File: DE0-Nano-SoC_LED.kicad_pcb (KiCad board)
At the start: 2 copper layers, 10 parts, among them J1 Conn_02x08_Odd_Even, J2 Conn_02x08_Odd_Even, J3 Conn_02x20_Odd_Even, J4 Conn_02x20_Odd_Even, U1 74HC245, U2 74HC245

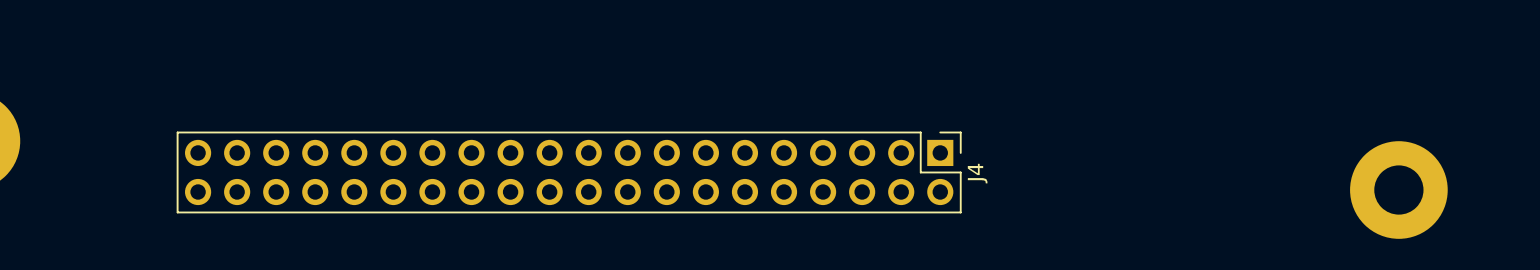
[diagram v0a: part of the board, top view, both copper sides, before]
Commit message: main DE0-Nano-SoC connectors are finally locked in their places
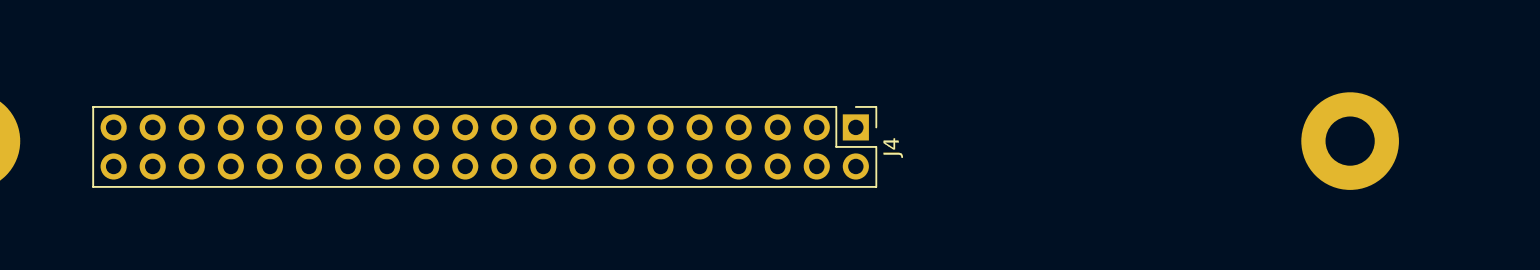
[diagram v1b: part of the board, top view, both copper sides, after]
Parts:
- moved J4 5.74 mm to (127.5, 131.3)
- moved REF** 4.61 mm to (159.7, 132.2)
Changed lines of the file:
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@@
     (links 10)
     (no_connects 10)
-    (area 69.899999 19.498 252.575001 143.322382)
+    (area 50.880001 18.804999 252.575001 142.922382)
     (thickness 1.6)
-    (drawings 3)
+    (drawings 9)
     (tracks 0)
     (zones 0)
@@
     )
   )
-  (module Pin_Headers:Pin_Header_Straight_2x20_Pitch2.54mm (layer F.Cu)
+  (module Pin_Headers:Pin_Header_Straight_2x20_Pitch2.54mm locked (layer F.Cu)
     (at 79.25 70.89 90)
     (descr "Through hole straight pin header, 2x20, 2.54mm pitch, double rows")
@@
     )
   )
-  (module Pin_Headers:Pin_Header_Straight_2x20_Pitch2.54mm (layer F.Cu)
-    (at 133 133 270)
+  (module Pin_Headers:Pin_Header_Straight_2x20_Pitch2.54mm locked (layer F.Cu)
+    (at 127.51 131.34 270)
     (descr "Through hole straight pin header, 2x20, 2.54mm pitch, double rows")
     (tags "Through hole pin header THT 2x20 2.54mm double row")
@@
   )
   (module wire_pad_custom:VIA-3.2x6.35mm (layer F.Cu)
-    (at 162.9 135.5)
+    (at 159.65 132.23)
     (fp_text reference REF** (at 0 4) (layer F.SilkS) hide
       (effects (font (size 1 1) (thickness 0.15)))
@@
       (effects (font (size 1 1) (thickness 0.15)))
     )
-    (pad 1 thru_hole circle (at -0.08 -0.09) (size 6.35 6.35) (drill 3.2) (layers *.Cu *.Mask)
+    (pad 1 thru_hole circle (at 0 0) (size 6.35 6.35) (drill 3.2) (layers *.Cu *.Mask)
       (net 42 GND))
   )
+  (gr_line (start 162.83 66.82) (end 162.83 135.41) (angle 90) (layer Eco1.User) (width 0.05))
+  (gr_line (start 66.82 66.82) (end 162.83 66.82) (angle 90) (layer Eco1.User) (width 0.05))
+  (gr_line (start 66.82 135.41) (end 162.83 135.41) (angle 90) (layer Eco1.User) (width 0.05))
+  (gr_line (start 66.82 66.82) (end 66.82 135.41) (angle 90) (layer Eco1.User) (width 0.05))
+  (dimension 57.51 (width 0.3) (layer Eco1.User)
+    (gr_text "57,510 mm" (at 98.755 123.82) (layer Eco1.User)
+      (effects (font (size 1.5 1.5) (thickness 0.3)))
+    )
+    (feature1 (pts (xy 127.51 132.23) (xy 127.51 122.47)))
+    (feature2 (pts (xy 70 132.23) (xy 70 122.47)))
+    (crossbar (pts (xy 70 125.17) (xy 127.51 125.17)))
+    (arrow1a (pts (xy 127.51 125.17) (xy 126.383496 125.756421)))
+    (arrow1b (pts (xy 127.51 125.17) (xy 126.383496 124.583579)))
+    (arrow2a (pts (xy 70 125.17) (xy 71.126504 125.756421)))
+    (arrow2b (pts (xy 70 125.17) (xy 71.126504 124.583579)))
+  )
+  (dimension 89.65 (width 0.3) (layer Eco1.User)
+    (gr_text "89,650 mm" (at 114.825 144.23) (layer Eco1.User)
+      (effects (font (size 1.5 1.5) (thickness 0.3)))
+    )
+    (feature1 (pts (xy 159.65 132.23) (xy 159.65 145.58)))
+    (feature2 (pts (xy 70 132.23) (xy 70 145.58)))
+    (crossbar (pts (xy 70 142.88) (xy 159.65 142.88)))
+    (arrow1a (pts (xy 159.65 142.88) (xy 158.523496 143.466421)))
+    (arrow1b (pts (xy 159.65 142.88) (xy 158.523496 142.293579)))
+    (arrow2a (pts (xy 70 142.88) (xy 71.126504 143.466421)))
+    (arrow2b (pts (xy 70 142.88) (xy 71.126504 142.293579)))
+  )
   (dimension 62.23 (width 0.3) (layer Eco1.User)

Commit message: still in connectors placement phase
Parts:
- removed REF** (x4): VIA-3.2x6.35mm, wire_pad_custom:VIA-3.2x6.35mm
- added J10: Conn_01x01, Mounting_Holes:MountingHole_3.2mm_M3_ISO7380_Pad, F.Cu at (70.0, 132.2)
- added J11: Conn_01x01, Mounting_Holes:MountingHole_3.2mm_M3_ISO7380_Pad, F.Cu at (159.7, 70.0)
- added J12: Conn_01x01, Mounting_Holes:MountingHole_3.2mm_M3_ISO7380_Pad, F.Cu at (69.5, 189.8)
- added J13: Conn_01x01, Mounting_Holes:MountingHole_3.2mm_M3_ISO7380_Pad, F.Cu at (158.3, 190.8)
- added J14: Conn_01x01, Mounting_Holes:MountingHole_3.2mm_M3_ISO7380_Pad, F.Cu at (70.0, 20.0)
- added J15: Conn_01x01, Mounting_Holes:MountingHole_3.2mm_M3_ISO7380_Pad, F.Cu at (159.7, 20.0)
- added J16: Conn_01x10, Pin_Headers:Pin_Header_Straight_1x10_Pitch2.54mm, F.Cu at (80.5, 79.0)
- added J17: Conn_01x08, Pin_Headers:Pin_Header_Straight_1x08_Pitch2.54mm, F.Cu at (108.9, 78.9)
- added J18: Conn_01x06, Pin_Headers:Pin_Header_Straight_1x06_Pitch2.54mm, F.Cu at (110.9, 120.3)
- added J19: Conn_01x08, Pin_Headers:Pin_Header_Straight_1x08_Pitch2.54mm, F.Cu at (88.0, 120.2)
- added J5: Conn_02x08_Odd_Even, Connectors_Multicomp:Multicomp_MC9A12-1634_2x08x2.54mm_Straight, F.Cu at (98.0, 45.0)
- added J6: Conn_02x08_Odd_Even, Connectors_Multicomp:Multicomp_MC9A12-1634_2x08x2.54mm_Straight, F.Cu at (134.0, 45.0)
- added J7: Conn_02x08_Odd_Even, Connectors_Multicomp:Multicomp_MC9A12-1634_2x08x2.54mm_Straight, F.Cu at (152.0, 45.0)
- added J8: Conn_01x01, Mounting_Holes:MountingHole_3.2mm_M3_ISO7380_Pad, F.Cu at (70.0, 70.0)
- added J9: Conn_01x01, Mounting_Holes:MountingHole_3.2mm_M3_ISO7380_Pad, F.Cu at (159.7, 132.2)
- added RN1: R_Pack04, Resistors_SMD:R_Array_Concave_4x0402, F.Cu at (105.1, 60.1)
- added RN2: R_Pack04, Resistors_SMD:R_Array_Concave_4x0402, F.Cu at (107.8, 60.1)
- moved J2 126.1 mm to (116.0, 45.0), turned to 90 degrees
- moved U1 41.4 mm to (106.5, 54.6)
- moved U2 38.5 mm to (80.2, 55.2)
- moved J1 2.68 mm to (79.0, 45.0)
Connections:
- J1 pad 16: Net-(J1-Pad16) -> GND
- J1 pad 4: Net-(J1-Pad4) -> GND
- J1 pad 8: Net-(J1-Pad8) -> GND
- J2 pad 16: Net-(J2-Pad16) -> GND
- J2 pad 4: Net-(J2-Pad4) -> GND
- J2 pad 8: Net-(J2-Pad8) -> GND
- J3 pad 11: Net-(J3-Pad11) -> VCC
- J3 pad 29: Net-(J3-Pad29) -> /3V3
- J4 pad 11: Net-(J4-Pad11) -> VCC
- J4 pad 29: Net-(J4-Pad29) -> /3V3
- U1 pad 1: Net-(U1-Pad1) -> VCC
- U1 pad 19: Net-(U1-Pad19) -> GND
- U2 pad 1: Net-(U2-Pad1) -> VCC
- U2 pad 19: Net-(U2-Pad19) -> GND
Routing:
- added copper zone on F.Cu, net GND
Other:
- board outline added: 98.1 x 178.3 mm
- net class Default: clearance 0.2 -> 0.18; trace_width 0.25 -> 0.18; via_dia 0.6 -> 0.7; via_drill 0.4 -> 0.3
- rule trace_clearance: 0.2 -> 0.18
- rule trace_min: 0.2 -> 0.18
- rule via_min_size: 0.4 -> 0.7

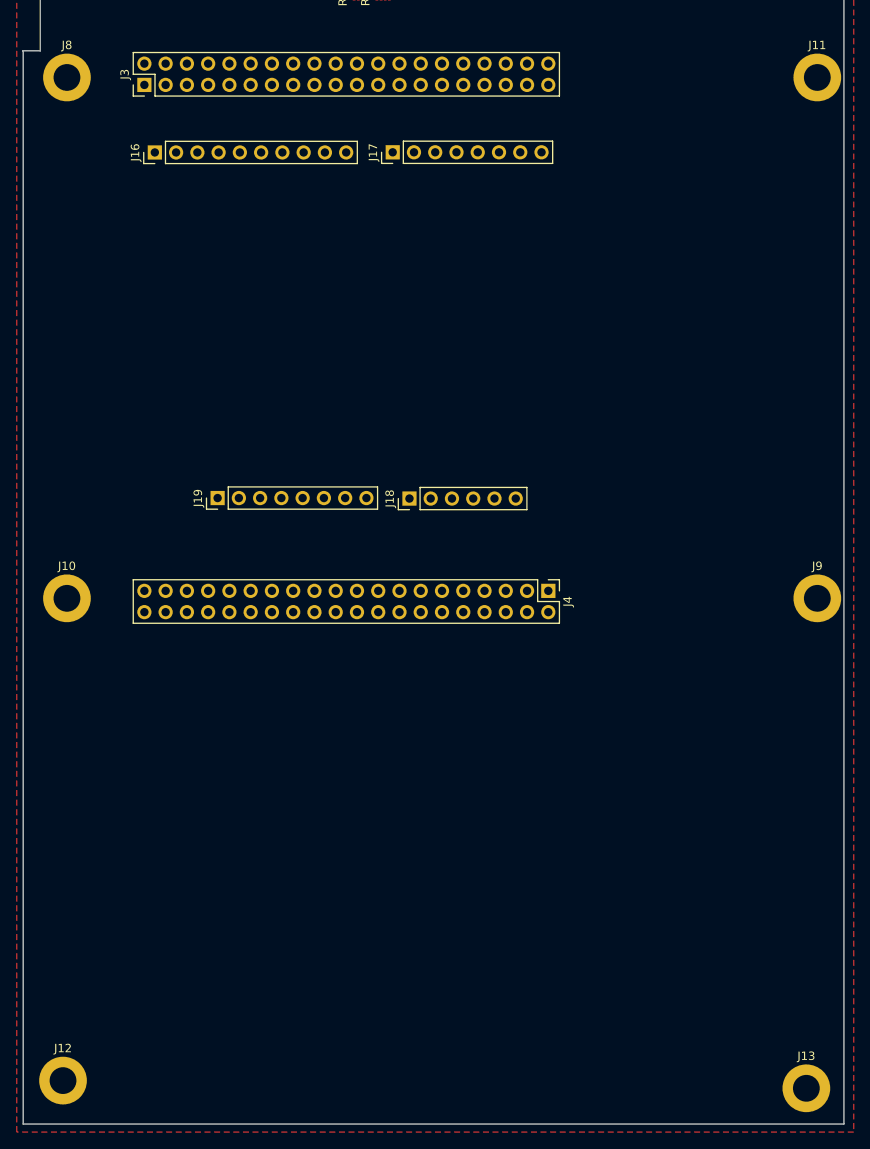
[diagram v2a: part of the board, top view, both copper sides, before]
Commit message: add more connectors
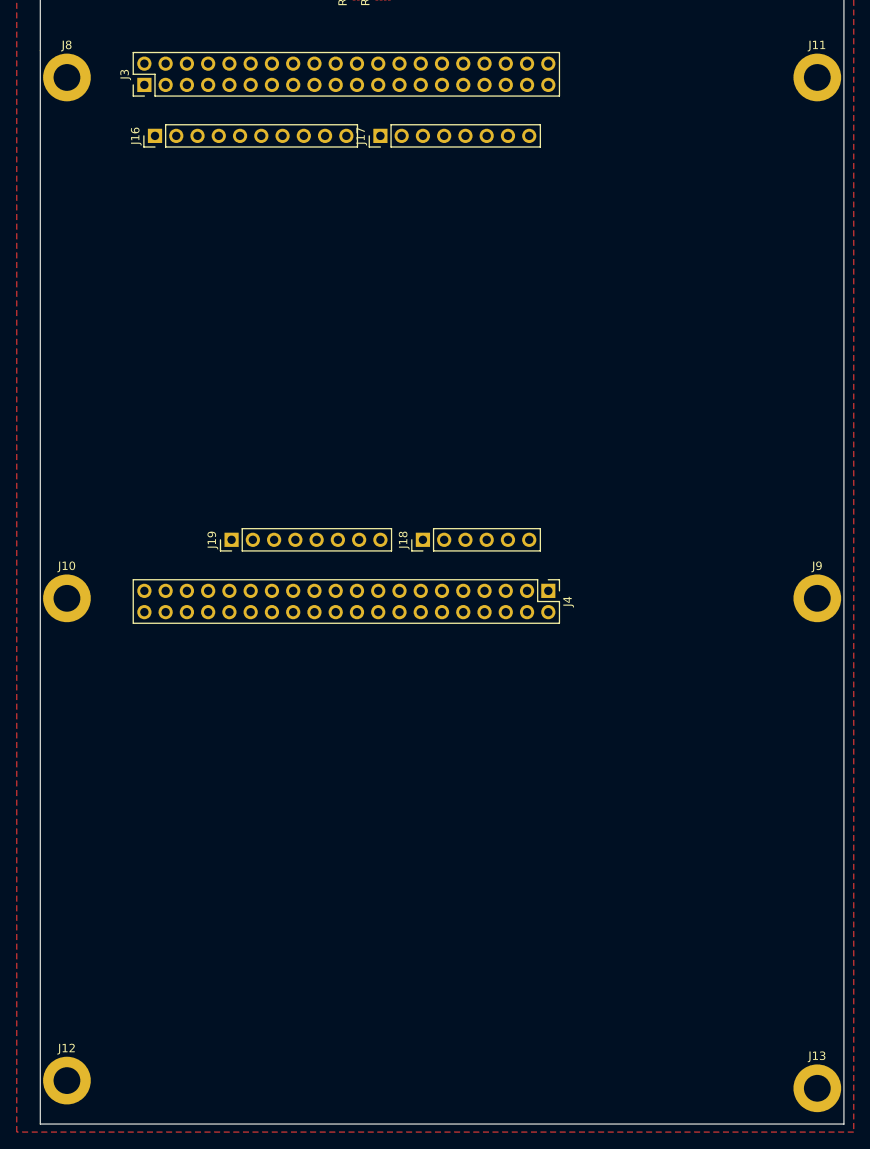
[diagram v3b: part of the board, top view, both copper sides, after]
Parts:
- moved J19 5.26 mm to (89.7, 125.2)
- moved J18 5.19 mm to (112.5, 125.2)
- moved J17 2.45 mm to (107.5, 77.0)
- moved J16 1.98 mm to (80.5, 77.0)
- moved J13 1.31 mm to (159.7, 190.8)
- moved J12 0.47 mm to (70.0, 189.8)
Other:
- board size 98.1 x 178.3 mm -> 96 x 178.3 mm
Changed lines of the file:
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@@
     (links 50)
     (no_connects 50)
-    (area 64.694999 16.754999 162.905001 195.115001)
+    (area 50.880001 15.195 164.37762 196.000001)
     (thickness 1.6)
-    (drawings 19)
+    (drawings 23)
     (tracks 0)
     (zones 0)
@@
     (37 F.SilkS user)
     (38 B.Mask user)
-    (39 F.Mask user)
+    (39 F.Mask user hide)
     (40 Dwgs.User user)
     (41 Cmts.User user)
@@
     (pad_to_mask_clearance 0.2)
     (aux_axis_origin 0 0)
+    (grid_origin 10.05 199.94)
     (visible_elements FFFFF75F)
     (pcbplotparams
@@
   )
   (module Mounting_Holes:MountingHole_3.2mm_M3_ISO7380_Pad (layer F.Cu)
-    (at 69.53 189.85)
+    (at 70 189.85)
     (descr "Mounting Hole 3.2mm, M3, ISO7380")
     (tags "mounting hole 3.2mm m3 iso7380")
@@
   )
   (module Mounting_Holes:MountingHole_3.2mm_M3_ISO7380_Pad (layer F.Cu)
-    (at 158.34 190.77)
+    (at 159.65 190.77)
     (descr "Mounting Hole 3.2mm, M3, ISO7380")
     (tags "mounting hole 3.2mm m3 iso7380")
@@
       (net 27 GND))
   )
-  (module Pin_Headers:Pin_Header_Straight_1x10_Pitch2.54mm (layer F.Cu)
-    (at 80.5 78.96 90)
+  (module Pin_Headers:Pin_Header_Straight_1x10_Pitch2.54mm locked (layer F.Cu)
+    (at 80.52 76.98 90)
     (descr "Through hole straight pin header, 1x10, 2.54mm pitch, single row")
     (tags "Through hole pin header THT 1x10 2.54mm single row")
@@
     )
   )
-  (module Pin_Headers:Pin_Header_Straight_1x08_Pitch2.54mm (layer F.Cu)
-    (at 108.92 78.94 90)
+  (module Pin_Headers:Pin_Header_Straight_1x08_Pitch2.54mm locked (layer F.Cu)
+    (at 107.45 76.98 90)
     (descr "Through hole straight pin header, 1x08, 2.54mm pitch, single row")
     (tags "Through hole pin header THT 1x08 2.54mm single row")
@@
     )
   )
-  (module Pin_Headers:Pin_Header_Straight_1x06_Pitch2.54mm (layer F.Cu)
-    (at 110.92 120.31 90)
+  (module Pin_Headers:Pin_Header_Straight_1x06_Pitch2.54mm locked (layer F.Cu)
+    (at 112.53 125.24 90)
     (descr "Through hole straight pin header, 1x06, 2.54mm pitch, single row")
     (tags "Through hole pin header THT 1x06 2.54mm single row")
@@
     )
   )
-  (module Pin_Headers:Pin_Header_Straight_1x08_Pitch2.54mm (layer F.Cu)
-    (at 88 120.25 90)
+  (module Pin_Headers:Pin_Header_Straight_1x08_Pitch2.54mm locked (layer F.Cu)
+    (at 89.67 125.24 90)
     (descr "Through hole straight pin header, 1x08, 2.54mm pitch, single row")
     (tags "Through hole pin header THT 1x08 2.54mm single row")
@@
     )
   )
-  (gr_line (start 64.77 66.82) (end 66.82 66.82) (angle 90) (layer Edge.Cuts) (width 0.15))
-  (gr_line (start 64.77 66.83) (end 64.77 66.82) (angle 90) (layer Edge.Cuts) (width 0.15))
-  (gr_line (start 64.77 66.84) (end 64.77 66.83) (angle 90) (layer Edge.Cuts) (width 0.15))
-  (gr_line (start 64.77 66.87) (end 64.77 66.84) (angle 90) (layer Edge.Cuts) (width 0.15))
-  (gr_line (start 64.77 195.04) (end 64.77 66.87) (angle 90) (layer Edge.Cuts) (width 0.15))
-  (gr_line (start 162.83 195.04) (end 64.77 195.04) (angle 90) (layer Edge.Cuts) (width 0.15))
+  (dimension 37.45 (width 0.3) (layer Eco1.User)
+    (gr_text "37,450 mm" (at 88.725 86.47) (layer Eco1.User)
+      (effects (font (size 1.5 1.5) (thickness 0.3)))
+    )
+    (feature1 (pts (xy 107.45 70) (xy 107.45 87.82)))
+    (feature2 (pts (xy 70 70) (xy 70 87.82)))
+    (crossbar (pts (xy 70 85.12) (xy 107.45 85.12)))
+    (arrow1a (pts (xy 107.45 85.12) (xy 106.323496 85.706421)))
+    (arrow1b (pts (xy 107.45 85.12) (xy 106.323496 84.533579)))
+    (arrow2a (pts (xy 70 85.12) (xy 71.126504 85.706421)))
+    (arrow2b (pts (xy 70 85.12) (xy 71.126504 84.533579)))
+  )
+  (gr_line (start 66.82 66.82) (end 66.82 195.04) (angle 90) (layer Edge.Cuts) (width 0.01))
+  (dimension 6.99 (width 0.3) (layer Eco1.User)
+    (gr_text "6,990 mm" (at 64.37 132 270) (layer Eco1.User)
+      (effects (font (size 1.5 1.5) (thickness 0.3)))
+    )
+    (feature1 (pts (xy 112.53 132.23) (xy 63.02 132.23)))
+    (feature2 (pts (xy 112.53 125.24) (xy 63.02 125.24)))
+    (crossbar (pts (xy 65.72 125.24) (xy 65.72 132.23)))
+    (arrow1a (pts (xy 65.72 132.23) (xy 65.133579 131.103496)))
+    (arrow1b (pts (xy 65.72 132.23) (xy 66.306421 131.103496)))
+    (arrow2a (pts (xy 65.72 125.24) (xy 65.133579 126.366504)))
+    (arrow2b (pts (xy 65.72 125.24) (xy 66.306421 126.366504)))
+  )
+  (dimension 55.25 (width 0.3) (layer Eco1.User)
+    (gr_text "55,250 mm" (at 61.65 104.605 270) (layer Eco1.User)
+      (effects (font (size 1.5 1.5) (thickness 0.3)))
+    )
+    (feature1 (pts (xy 107.35 132.23) (xy 60.3 132.23)))
+    (feature2 (pts (xy 107.35 76.98) (xy 60.3 76.98)))
+    (crossbar (pts (xy 63 76.98) (xy 63 132.23)))
+    (arrow1a (pts (xy 63 132.23) (xy 62.413579 131.103496)))
+    (arrow1b (pts (xy 63 132.23) (xy 63.586421 131.103496)))
+    (arrow2a (pts (xy 63 76.98) (xy 62.413579 78.106504)))
+    (arrow2b (pts (xy 63 76.98) (xy 63.586421 78.106504)))
+  )
+  (gr_line (start 10 76.98) (end 73.94 76.98) (angle 90) (layer Eco1.User) (width 0.01))
+  (dimension 42.53 (width 0.3) (layer Eco1.User)
+    (gr_text "42,530 mm" (at 91.265 120.58) (layer Eco1.User)
+      (effects (font (size 1.5 1.5) (thickness 0.3)))
+    )
+    (feature1 (pts (xy 112.53 132.23) (xy 112.53 119.23)))
+    (feature2 (pts (xy 70 132.23) (xy 70 119.23)))
+    (crossbar (pts (xy 70 121.93) (xy 112.53 121.93)))
+    (arrow1a (pts (xy 112.53 121.93) (xy 111.403496 122.516421)))
+    (arrow1b (pts (xy 112.53 121.93) (xy 111.403496 121.343579)))
+    (arrow2a (pts (xy 70 121.93) (xy 71.126504 122.516421)))
+    (arrow2b (pts (xy 70 121.93) (xy 71.126504 121.343579)))
+  )
+  (dimension 19.67 (width 0.3) (layer Eco1.User)
+    (gr_text "19,670 mm" (at 79.835 126.73) (layer Eco1.User)
+      (effects (font (size 1.5 1.5) (thickness 0.3)))
+    )
+    (feature1 (pts (xy 89.67 132.23) (xy 89.67 125.38)))
+    (feature2 (pts (xy 70 132.23) (xy 70 125.38)))
+    (crossbar (pts (xy 70 128.08) (xy 89.67 128.08)))
+    (arrow1a (pts (xy 89.67 128.08) (xy 88.543496 128.666421)))
+    (arrow1b (pts (xy 89.67 128.08) (xy 88.543496 127.493579)))
+    (arrow2a (pts (xy 70 128.08) (xy 71.126504 128.666421)))
+    (arrow2b (pts (xy 70 128.08) (xy 71.126504 127.493579)))
+  )
+  (dimension 57.51 (width 0.3) (layer Eco1.User)
+    (gr_text "57,510 mm" (at 98.755 139.86) (layer Eco1.User)
+      (effects (font (size 1.5 1.5) (thickness 0.3)))
+    )
+    (feature1 (pts (xy 127.51 132.23) (xy 127.51 141.21)))
+    (feature2 (pts (xy 70 132.23) (xy 70 141.21)))
+    (crossbar (pts (xy 70 138.51) (xy 127.51 138.51)))
+    (arrow1a (pts (xy 127.51 138.51) (xy 126.383496 139.096421)))
+    (arrow1b (pts (xy 127.51 138.51) (xy 126.383496 137.923579)))
+    (arrow2a (pts (xy 70 138.51) (xy 71.126504 139.096421)))
+    (arrow2b (pts (xy 70 138.51) (xy 71.126504 137.923579)))
+  )
+  (dimension 62.23 (width 0.3) (layer Eco1.User)
+    (gr_text "62,230 mm" (at 168.21 101.115 90) (layer Eco1.User)
+      (effects (font (size 1.5 1.5) (thickness 0.3)))
+    )
+    (feature1 (pts (xy 159.65 70) (xy 169.56 70)))
+    (feature2 (pts (xy 159.65 132.23) (xy 169.56 132.23)))
+    (crossbar (pts (xy 166.86 132.23) (xy 166.86 70)))
+    (arrow1a (pts (xy 166.86 70) (xy 167.446421 71.126504)))
+    (arrow1b (pts (xy 166.86 70) (xy 166.273579 71.126504)))
+    (arrow2a (pts (xy 166.86 132.23) (xy 167.446421 131.103496)))
+    (arrow2b (pts (xy 166.86 132.23) (xy 166.273579 131.103496)))
+  )
+  (dimension 10.52 (width 0.3) (layer Eco1.User)
+    (gr_text "10,520 mm" (at 77.8 82.69) (layer Eco1.User)
+      (effects (font (size 1.5 1.5) (thickness 0.3)))
+    )
+    (feature1 (pts (xy 80.52 70) (xy 80.52 84.04)))
+    (feature2 (pts (xy 70 70) (xy 70 84.04)))
+    (crossbar (pts (xy 70 81.34) (xy 80.52 81.34)))
+    (arrow1a (pts (xy 80.52 81.34) (xy 79.393496 81.926421)))
+    (arrow1b (pts (xy 80.52 81.34) (xy 79.393496 80.753579)))
+    (arrow2a (pts (xy 70 81.34) (xy 71.126504 81.926421)))
+    (arrow2b (pts (xy 70 81.34) (xy 71.126504 80.753579)))
+  )
+  (gr_line (start 162.83 195.04) (end 66.82 195.04) (angle 90) (layer Edge.Cuts) (width 0.01))
   (gr_line (start 162.83 16.76) (end 162.83 195.04) (angle 90) (layer Edge.Cuts) (width 0.01))
   (gr_line (start 66.82 16.76) (end 162.83 16.76) (angle 90) (layer Edge.Cuts) (width 0.01))
@@
   (gr_line (start 66.82 135.41) (end 162.83 135.41) (angle 90) (layer Eco1.User) (width 0.05))
   (gr_line (start 66.82 66.82) (end 66.82 135.41) (angle 90) (layer Eco1.User) (width 0.05))
-  (dimension 57.51 (width 0.3) (layer Eco1.User)
-    (gr_text "57,510 mm" (at 98.755 123.82) (layer Eco1.User)
-      (effects (font (size 1.5 1.5) (thickness 0.3)))
-    )
-    (feature1 (pts (xy 127.51 132.23) (xy 127.51 122.47)))
-    (feature2 (pts (xy 70 132.23) (xy 70 122.47)))
-    (crossbar (pts (xy 70 125.17) (xy 127.51 125.17)))
-    (arrow1a (pts (xy 127.51 125.17) (xy 126.383496 125.756421)))
-    (arrow1b (pts (xy 127.51 125.17) (xy 126.383496 124.583579)))
-    (arrow2a (pts (xy 70 125.17) (xy 71.126504 125.756421)))
-    (arrow2b (pts (xy 70 125.17) (xy 71.126504 124.583579)))
-  )
   (dimension 89.65 (width 0.3) (layer Eco1.User)
     (gr_text "89,650 mm" (at 114.825 144.23) (layer Eco1.User)
